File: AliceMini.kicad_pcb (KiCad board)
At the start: 2 copper layers, 26 x 52 mm, 28 parts, among them IC1 OPA1642AIDR

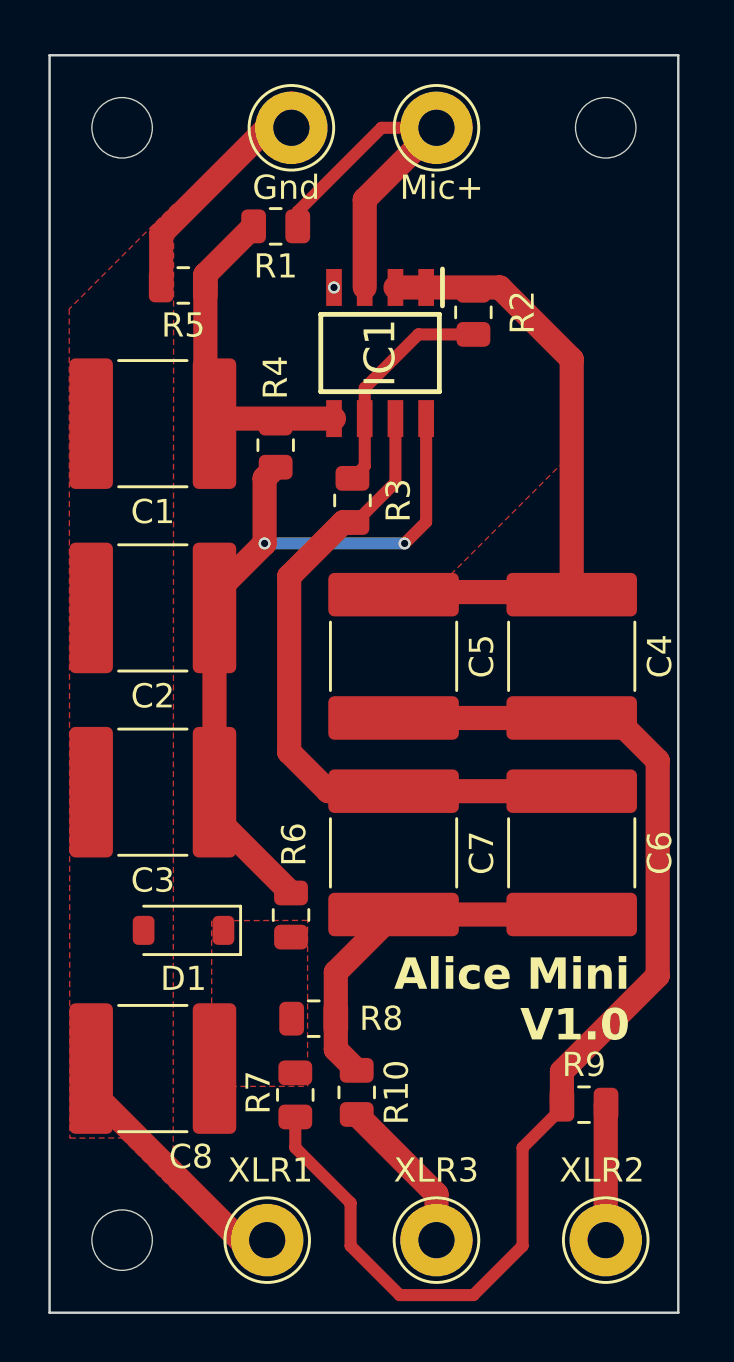
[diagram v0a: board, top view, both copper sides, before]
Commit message: Reduce board size and snap to mm instead of mils
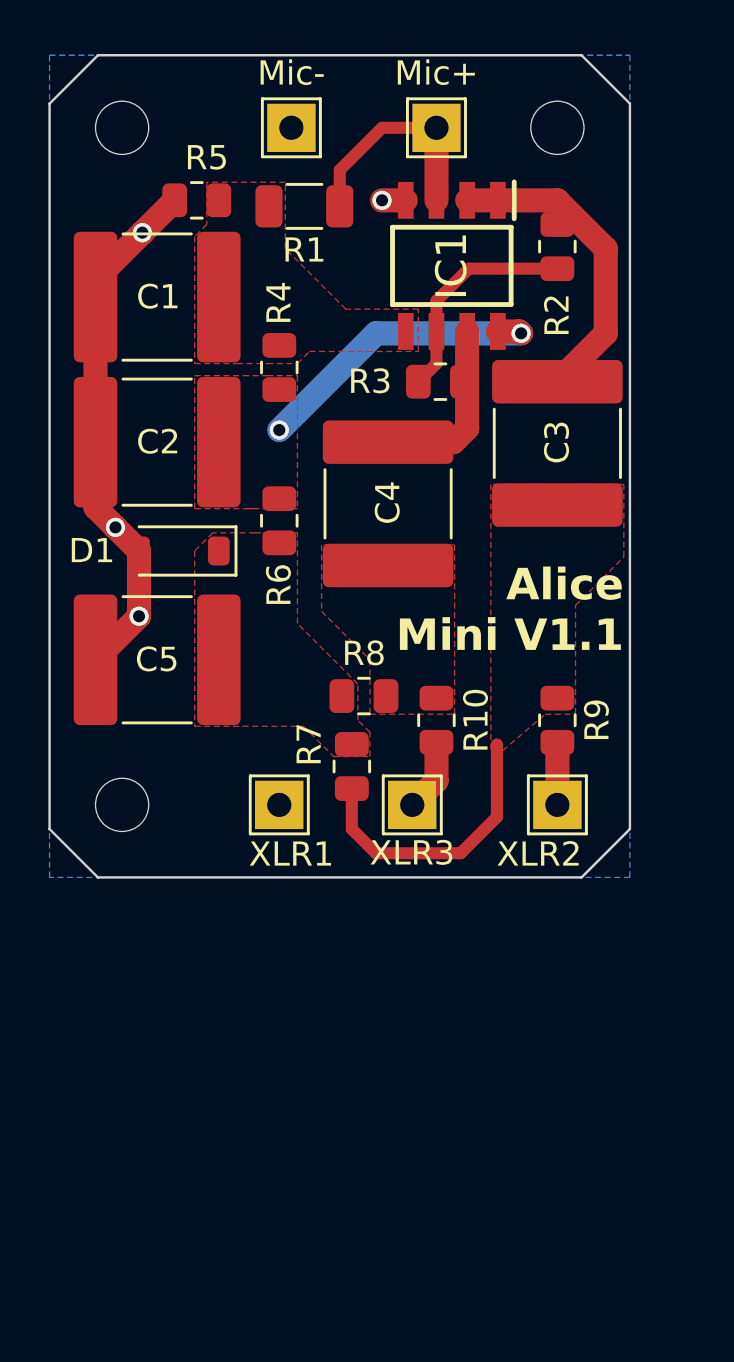
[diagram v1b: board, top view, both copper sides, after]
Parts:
- removed C6, C7, C8: 22uF, Capacitor_SMD:C_2220_5750Metric
- removed REF** (x3): MountingHole_2.5mm, MountingHole:MountingHole_2.5mm
- added H6: XLR2, TestPoint:TestPoint_THTPad_2.0x2.0mm_Drill1.0mm, F.Cu at (121.0, 131.0)
- added H7: XLR3, TestPoint:TestPoint_THTPad_2.0x2.0mm_Drill1.0mm, F.Cu at (115.0, 131.0)
- added H8: XLR1, TestPoint:TestPoint_THTPad_2.0x2.0mm_Drill1.0mm, F.Cu at (109.5, 131.0)
- H1: value Mic+ -> MountingHole; footprint TestPoint:TestPoint_THTPad_D3.0mm_Drill1.5mm -> MountingHole:MountingHole_2.2mm_M2
- H2: value Mic- -> MountingHole; footprint TestPoint:TestPoint_THTPad_D3.0mm_Drill1.5mm -> MountingHole:MountingHole_2.2mm_M2
- H3: value XLR 3 -> MountingHole; footprint TestPoint:TestPoint_THTPad_D3.0mm_Drill1.5mm -> MountingHole:MountingHole_2.2mm_M2
- H4: value XLR 2 -> Mic+; footprint TestPoint:TestPoint_THTPad_D3.0mm_Drill1.5mm -> TestPoint:TestPoint_THTPad_2.0x2.0mm_Drill1.0mm
- H5: value XLR 1 -> Mic-; footprint TestPoint:TestPoint_THTPad_D3.0mm_Drill1.5mm -> TestPoint:TestPoint_THTPad_2.0x2.0mm_Drill1.0mm
- R1: value 1G -> 800M; footprint Resistor_SMD:R_0805_2012Metric -> Resistor_SMD:R_1206_3216Metric
- R6: value 200 -> 400
- moved H4 46.5 mm to (116.0, 103.0)
- moved H5 46.0 mm to (110.0, 103.0)
- moved H3 22.2 mm to (103.0, 131.0)
- moved C3 22.1 mm to (121.0, 116.0), turned to -90 degrees
- moved R6 16.3 mm to (109.5, 119.2)
- moved R9 15.9 mm to (121.0, 127.5), turned to -90 degrees
- moved R10 15.7 mm to (116.0, 127.5)
- moved D1 15.7 mm to (105.3, 120.5)
- moved R7 13.8 mm to (112.5, 129.4)
- moved R8 13.5 mm to (113.0, 126.5)
- moved H1 13.0 mm to (103.0, 103.0)
- moved H2 11.0 mm to (121.0, 103.0)
- moved C4 9.87 mm to (114.0, 118.5)
- moved C5 9.78 mm to (104.5, 125.0), turned to 180 degrees
- moved C2 6.86 mm to (104.5, 116.0)
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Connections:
- C3 pad 1: Net-(IC1-V+) -> Net-(IC1--IN_A)
- C3 pad 2: GND -> Net-(C3-Pad2)
- C4 pad 1: Net-(IC1--IN_A) -> Net-(IC1-OUT_B)
- C5 pad 1: Net-(IC1--IN_A) -> Net-(D1-K)
- C5 pad 2: Net-(C4-Pad2) -> GND
- H4 pad 1: Net-(H4-Pad1) -> Net-(IC1-+IN_A)
- R10 pad 1: Net-(C6-Pad2) -> Net-(C4-Pad2)
- R10 pad 2: Net-(H3-Pad1) -> Net-(H7-Pad1)
- R7 pad 1: Net-(C4-Pad2) -> Net-(C3-Pad2)
- R8 pad 1: Net-(C6-Pad2) -> Net-(C4-Pad2)
- R9 pad 1: Net-(C4-Pad2) -> Net-(C3-Pad2)
- R9 pad 2: Net-(H4-Pad1) -> Net-(H6-Pad1)
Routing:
- net Net-(C4-Pad2): track 49.1 -> 0.00 mm
- net Net-(IC1-OUT_B): track 28.3 -> 7.51 mm
- net Net-(IC1-V+): track 32.3 -> 12.6 mm
- net Net-(C6-Pad2): track 15.2 -> 0.00 mm
- net Net-(IC1-+IN_B): track 14.2 -> 0.00 mm
- net Net-(IC1--IN_A): track 25.2 -> 12.9 mm
- net Net-(C3-Pad2): track 0.00 -> 11.7 mm
- net Net-(IC1-+IN_A): track 15.6 -> 9.22 mm
- net Net-(H3-Pad1): track 6.35 -> 0.00 mm
- net Net-(H4-Pad1): track 5.61 -> 0.00 mm
- net GND: track 19.6 -> 22.8 mm, vias 1 -> 4
- net Net-(H7-Pad1): track 0.00 -> 3.00 mm
- net Net-(H6-Pad1): track 0.00 -> 2.59 mm
- added copper zone on F.Cu, net Net-(C3-Pad2)
- added copper zone on F.Cu, net Net-(C4-Pad2)
- added copper zone on F.Cu, net Net-(IC1-+IN_B)
- added copper zone on F.Cu, net Net-(IC1-V+)
- removed copper zone on F.Cu, net GND
- removed copper zone on F.Cu, net Net-(IC1--IN_A)
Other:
- board size 26 x 52 mm -> 24 x 34 mm
- board text added: "Alice Mini V1.1"
- board text removed: "Alice Mini V1.0"
- board text removed: "Gnd"
- board text removed: "Mic+"
- board text removed: "XLR1"
- board text removed: "XLR2"
- board text removed: "XLR3"

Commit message: Move PCB to origin
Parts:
- moved C1 141.4 mm to (4.45, 10.0)
- moved C2 141.4 mm to (4.45, 16.0)
- moved C3 141.4 mm to (21.0, 16.1)
- moved C4 141.4 mm to (14.0, 18.6)
- moved C5 141.4 mm to (4.45, 25.0)
- moved D1 141.4 mm to (5.35, 20.5)
- moved H1 141.4 mm to (3.00, 3.00)
- moved H2 141.4 mm to (21.0, 3.00)
- moved H3 141.4 mm to (3.00, 31.0)
- moved H4 141.4 mm to (16.0, 3.00)
- moved H5 141.4 mm to (10.0, 3.00)
- moved H6 141.4 mm to (21.0, 31.0)
- moved H7 141.4 mm to (15.0, 31.0)
- moved H8 141.4 mm to (9.50, 31.0)
- moved IC1 141.4 mm to (16.6, 8.71)
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
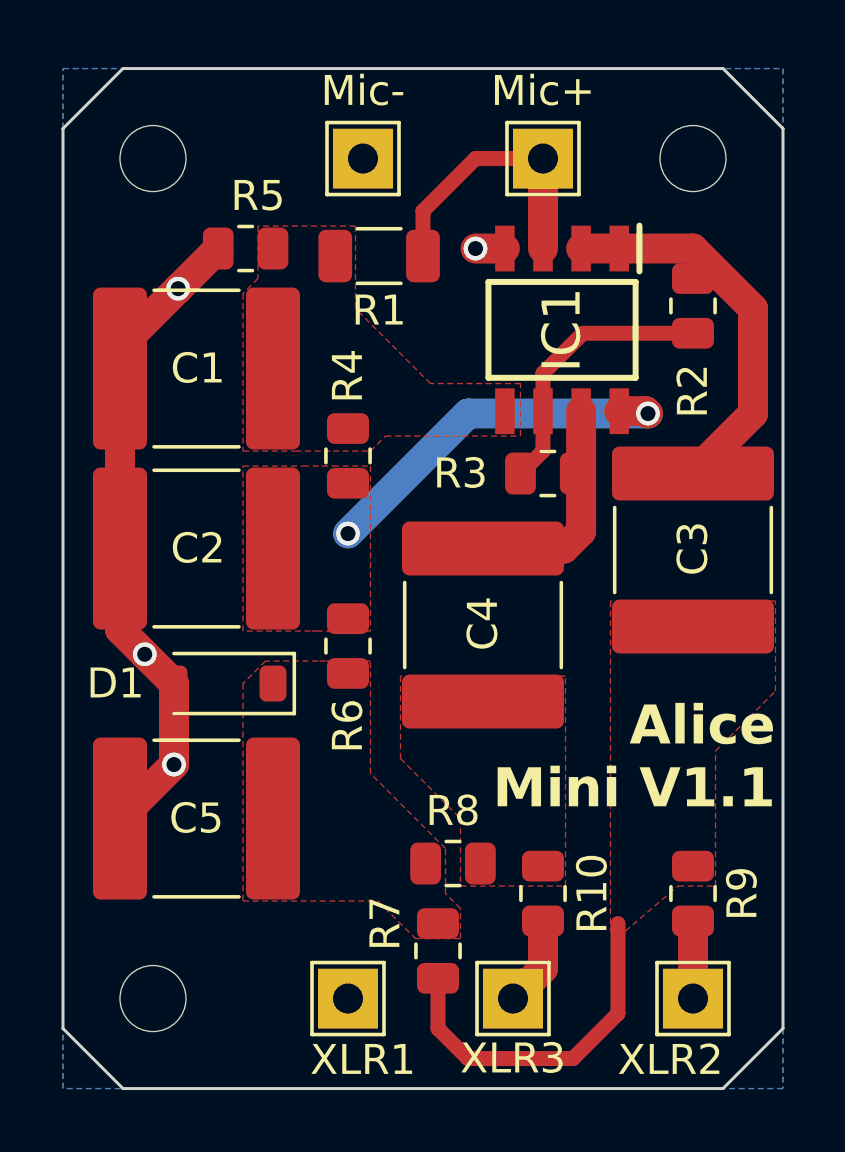
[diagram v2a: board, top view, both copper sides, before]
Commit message: fix: Updated high impedance resistor to 1G again
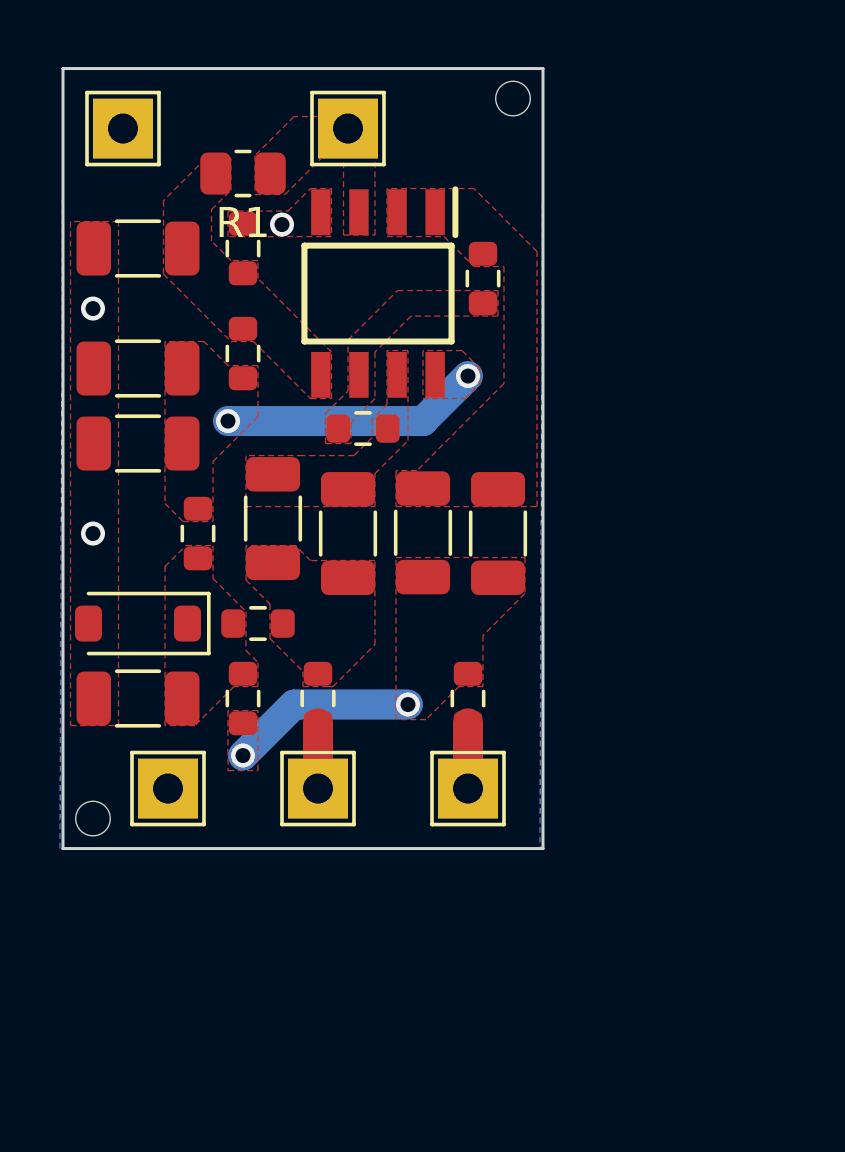
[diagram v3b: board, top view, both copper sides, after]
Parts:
- removed H1, H2, H3: MountingHole, MountingHole:MountingHole_2.2mm_M2
- added C6: 10uF, Capacitor_SMD:C_1206_3216Metric, F.Cu at (9.50, 15.5)
- added C7: 10uF, Capacitor_SMD:C_1206_3216Metric, F.Cu at (7.00, 15.0)
- added C8: 10uF, Capacitor_SMD:C_1206_3216Metric, F.Cu at (2.50, 21.0)
- added REF**: JLCPCB_Tooling_Hole, Project_Library:JLCPCB_Tooling_Hole, F.Cu at (15.0, 1.00)
- added REF**: JLCPCB_Tooling_Hole, Project_Library:JLCPCB_Tooling_Hole, F.Cu at (1.00, 25.0)
- C1, C2, C3, C4, C5: value 22uF -> 10uF; footprint Capacitor_SMD:C_2220_5750Metric -> Capacitor_SMD:C_1206_3216Metric
- R1: value 800M -> 1000M; footprint Resistor_SMD:R_1206_3216Metric -> Resistor_SMD:R_0805_2012Metric
- R10, R2, R3, R4, R5, R7, R8, R9: footprint Resistor_SMD:R_0805_2012Metric -> Resistor_SMD:R_0603_1608Metric
- R6: value 400 -> 470; footprint Resistor_SMD:R_0805_2012Metric -> Resistor_SMD:R_0603_1608Metric
- moved C3 18.8 mm to (2.50, 12.5), turned to 0 degrees
- moved C5 12.2 mm to (12.0, 15.5), turned to -90 degrees
- moved R7 10.6 mm to (6.00, 21.0)
- moved R8 10.3 mm to (6.50, 18.5)
- moved H6 10.3 mm to (13.5, 24.0)
- moved R10 9.92 mm to (8.50, 21.0)
- moved R9 9.92 mm to (13.5, 21.0)
- moved H7 9.55 mm to (8.50, 24.0)
- moved H8 9.22 mm to (3.50, 24.0)
- moved H5 8.06 mm to (2.00, 2.00)
- moved R2 7.06 mm to (14.0, 7.00)
- moved H4 6.58 mm to (9.50, 2.00)
- moved R3 6.34 mm to (10.0, 12.0)
- moved C2 6.31 mm to (2.50, 10.0), turned to 0 degrees
- moved IC1 6.25 mm to (10.5, 7.50)
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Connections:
- C1 pad 1: Net-(IC1-+IN_B) -> GND
- C1 pad 2: GND -> Net-(IC1-+IN_B)
- C2 pad 1: Net-(IC1-V+) -> GND
- C2 pad 2: GND -> Net-(IC1-V+)
- C3 pad 1: Net-(IC1--IN_A) -> GND
- C3 pad 2: Net-(C3-Pad2) -> Net-(IC1-V+)
- C4 pad 1: Net-(IC1-OUT_B) -> Net-(IC1--IN_A)
- C5 pad 1: Net-(D1-K) -> Net-(IC1--IN_A)
- C5 pad 2: GND -> Net-(C4-Pad2)
- R10 pad 1: Net-(C4-Pad2) -> Net-(C6-Pad2)
- R7 pad 1: Net-(C3-Pad2) -> Net-(C4-Pad2)
- R8 pad 1: Net-(C4-Pad2) -> Net-(C6-Pad2)
- R9 pad 1: Net-(C3-Pad2) -> Net-(C4-Pad2)
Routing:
- net GND: track 22.8 -> 0.00 mm, vias 4 -> 3
- net Net-(IC1--IN_A): track 12.9 -> 0.00 mm
- net Net-(C3-Pad2): track 11.7 -> 0.00 mm
- net Net-(IC1-+IN_A): track 9.22 -> 0.00 mm
- net Net-(IC1--IN_B): track 9.20 -> 0.00 mm
- net Net-(IC1-OUT_B): track 7.51 -> 0.00 mm
- net Net-(C4-Pad2): track 0.00 -> 6.20 mm, vias 0 -> 2
- net Net-(IC1-V+): track 12.6 -> 8.62 mm
- net Net-(H7-Pad1): track 3.00 -> 2.18 mm
- added copper zone on F.Cu, net GND
- added copper zone on F.Cu, net Net-(C6-Pad2)
- added copper zone on F.Cu, net Net-(IC1-+IN_A)
- added copper zone on F.Cu, net Net-(IC1--IN_A)
- added copper zone on F.Cu, net Net-(IC1--IN_B)
- added copper zone on F.Cu, net Net-(IC1-OUT_B)
- removed copper zone on F.Cu, net Net-(C3-Pad2)
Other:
- board size 24 x 34 mm -> 16 x 26 mm
- board text added: "+"
- board text added: "-"
- board text added: "1"
- board text added: "2"
- board text added: "3"
- board text added: "Alice Mini V1.2"
- board text added: "Designed by Oran Ellis"
- board text added: "Mic"
- board text added: "XLR"
- board text removed: "Alice Mini V1.1"
